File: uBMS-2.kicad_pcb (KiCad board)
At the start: 4 copper layers, 60 x 90 mm, 0 parts

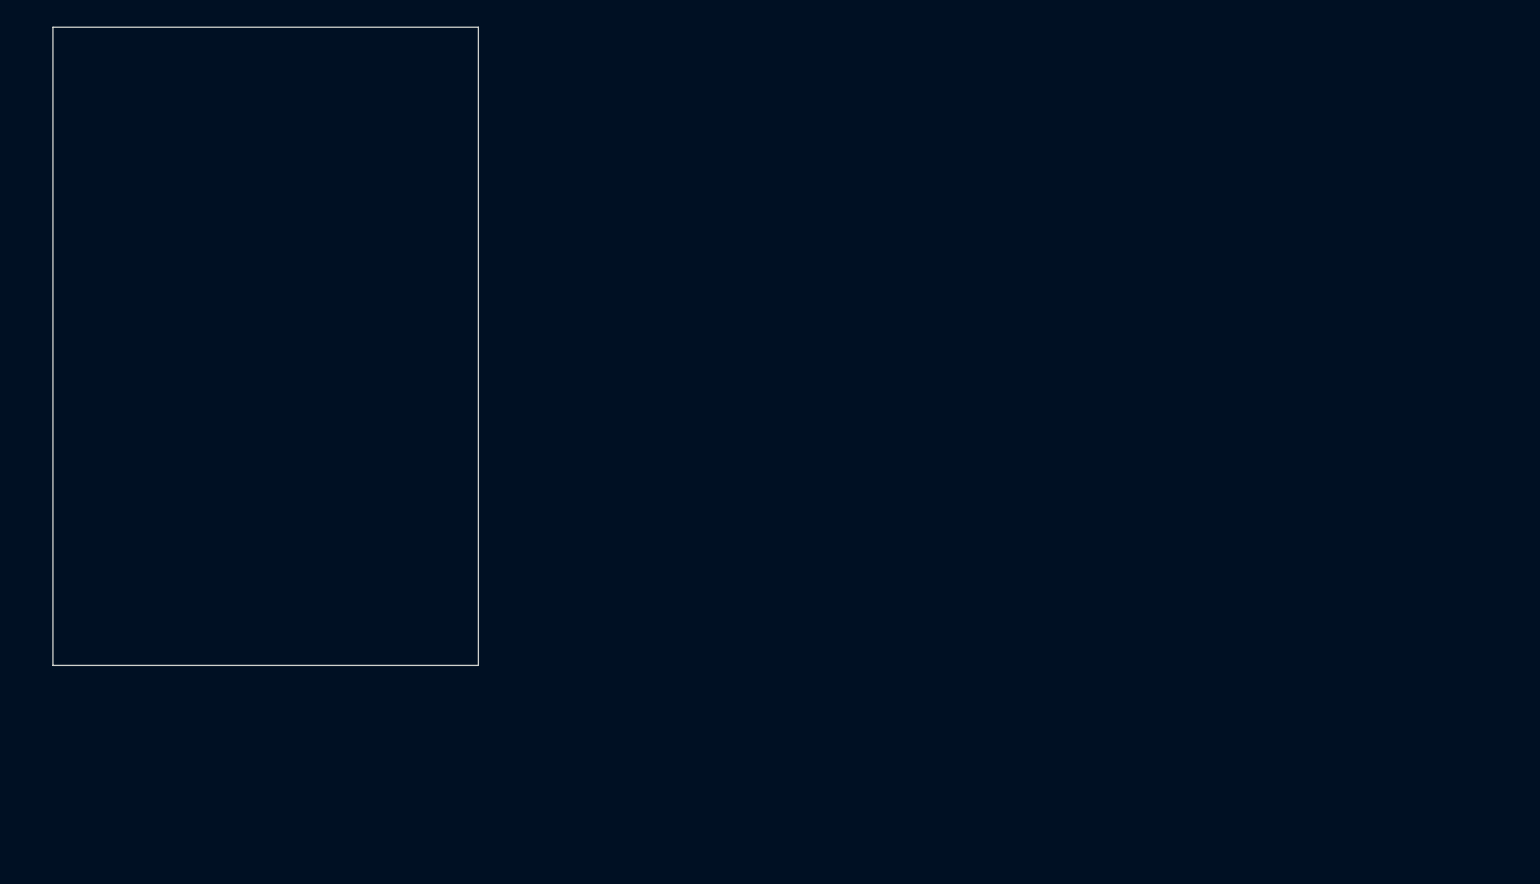
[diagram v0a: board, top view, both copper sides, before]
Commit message: Using Molex Milli Grid Connector for 14 pin
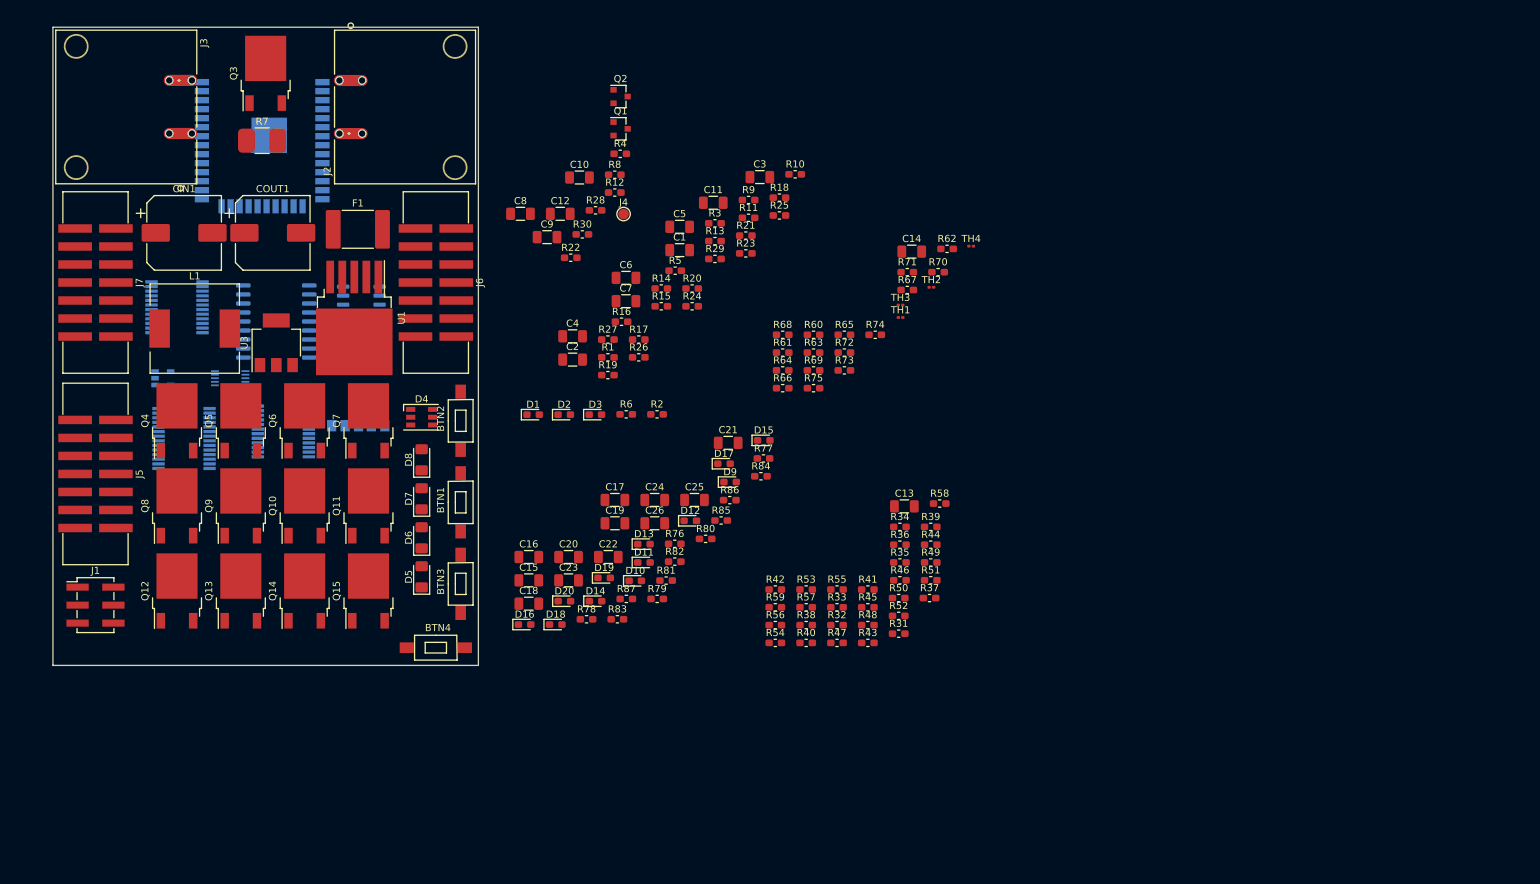
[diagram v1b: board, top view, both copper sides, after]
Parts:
- added BTN1: Reset, Button_Switch_SMD:PTS636_SM43_SMTR_LFS_6mm_3,5mm, F.Cu at (77.5, 87.0)
- added BTN2: Program, Button_Switch_SMD:PTS636_SM43_SMTR_LFS_6mm_3,5mm, F.Cu at (77.5, 75.5)
- added BTN3: Input_1, Button_Switch_SMD:PTS636_SM43_SMTR_LFS_6mm_3,5mm, F.Cu at (77.5, 98.5)
- added BTN4: Input_2, Button_Switch_SMD:PTS636_SM43_SMTR_LFS_6mm_3,5mm, F.Cu at (74.0, 107.5)
- added C1: 0.1uF, Capacitor_SMD:C_1206_3216Metric, F.Cu at (108.4, 51.4)
- added C10: 0.1uF, Capacitor_SMD:C_1206_3216Metric, F.Cu at (94.3, 41.2)
- added C11: 0.1uF, Capacitor_SMD:C_1206_3216Metric, F.Cu at (113.1, 44.8)
- added C12: 0.1uF, Capacitor_SMD:C_1206_3216Metric, F.Cu at (91.5, 46.3)
- added C13: 0.1uF, Capacitor_SMD:C_1206_3216Metric, F.Cu at (140.1, 87.6)
- added C14: 0.1uF, Capacitor_SMD:C_1206_3216Metric, F.Cu at (141.1, 51.6)
- added C15: 10nF, Capacitor_SMD:C_1206_3216Metric, F.Cu at (87.1, 98.0)
- added C16: 10nF, Capacitor_SMD:C_1206_3216Metric, F.Cu at (87.1, 94.7)
- added C17: 10nF, Capacitor_SMD:C_1206_3216Metric, F.Cu at (99.3, 86.7)
- added C18: 10nF, Capacitor_SMD:C_1206_3216Metric, F.Cu at (87.1, 101.3)
- added C19: 10nF, Capacitor_SMD:C_1206_3216Metric, F.Cu at (99.3, 90.0)
- added C2: 10uF, Capacitor_SMD:C_1206_3216Metric, F.Cu at (93.3, 66.9)
- added C20: 10nF, Capacitor_SMD:C_1206_3216Metric, F.Cu at (92.7, 94.7)
- added C21: 10nF, Capacitor_SMD:C_1206_3216Metric, F.Cu at (115.2, 78.6)
- added C22: 10nF, Capacitor_SMD:C_1206_3216Metric, F.Cu at (98.3, 94.7)
- added C23: 10nF, Capacitor_SMD:C_1206_3216Metric, F.Cu at (92.7, 98.0)
- added C24: 10nF, Capacitor_SMD:C_1206_3216Metric, F.Cu at (104.9, 86.7)
- added C25: 10nF, Capacitor_SMD:C_1206_3216Metric, F.Cu at (110.5, 86.7)
- added C26: 10nF, Capacitor_SMD:C_1206_3216Metric, F.Cu at (104.9, 90.0)
- added C3: 0.1uF, Capacitor_SMD:C_1206_3216Metric, F.Cu at (119.7, 41.1)
- added C4: 0.1uF, Capacitor_SMD:C_1206_3216Metric, F.Cu at (93.3, 63.6)
- added C5: 2.2uF, Capacitor_SMD:C_1206_3216Metric, F.Cu at (108.4, 48.1)
- added C6: 1uF, Capacitor_SMD:C_1206_3216Metric, F.Cu at (100.8, 55.3)
- added C7: 1uF, Capacitor_SMD:C_1206_3216Metric, F.Cu at (100.8, 58.6)
- added C8: 0.1uF, Capacitor_SMD:C_1206_3216Metric, F.Cu at (85.9, 46.3)
- added C9: 0.1uF, Capacitor_SMD:C_1206_3216Metric, F.Cu at (89.7, 49.6)
- added CIN1: 100uF 60V, Capacitor_SMD:CP_Elec_10x10, F.Cu at (38.5, 49.0)
- added COUT1: 1000uF, Capacitor_SMD:CP_Elec_10x10, F.Cu at (51.0, 49.0)
- added D1: D, Diode_SMD:D_0603_1608Metric_Pad1.05x0.95mm_HandSolder, F.Cu at (87.7, 74.6)
- added D10: D, Diode_SMD:D_0603_1608Metric_Pad1.05x0.95mm_HandSolder, F.Cu at (102.1, 98.1)
- added D11: D, Diode_SMD:D_0603_1608Metric_Pad1.05x0.95mm_HandSolder, F.Cu at (103.4, 95.5)
- added D12: D, Diode_SMD:D_0603_1608Metric_Pad1.05x0.95mm_HandSolder, F.Cu at (109.9, 89.6)
- added D13: D, Diode_SMD:D_0603_1608Metric_Pad1.05x0.95mm_HandSolder, F.Cu at (103.4, 92.9)
- added D14: D, Diode_SMD:D_0603_1608Metric_Pad1.05x0.95mm_HandSolder, F.Cu at (96.5, 100.9)
- added D15: D, Diode_SMD:D_0603_1608Metric_Pad1.05x0.95mm_HandSolder, F.Cu at (120.3, 78.3)
- added D16: D, Diode_SMD:D_0603_1608Metric_Pad1.05x0.95mm_HandSolder, F.Cu at (86.5, 104.2)
- added D17: D, Diode_SMD:D_0603_1608Metric_Pad1.05x0.95mm_HandSolder, F.Cu at (114.6, 81.6)
- added D18: D, Diode_SMD:D_0603_1608Metric_Pad1.05x0.95mm_HandSolder, F.Cu at (90.9, 104.2)
- added D19: D, Diode_SMD:D_0603_1608Metric_Pad1.05x0.95mm_HandSolder, F.Cu at (97.7, 97.7)
- added D2: D, Diode_SMD:D_0603_1608Metric_Pad1.05x0.95mm_HandSolder, F.Cu at (92.1, 74.6)
- added D20: D, Diode_SMD:D_0603_1608Metric_Pad1.05x0.95mm_HandSolder, F.Cu at (92.1, 100.9)
- added D3: D, Diode_SMD:D_0603_1608Metric_Pad1.05x0.95mm_HandSolder, F.Cu at (96.5, 74.6)
- added D4: CLX6F-FKC, LED_SMD:LED_RGB_PLCC-6, F.Cu at (72.0, 75.0)
- added D5: LED, LED_SMD:LED_1206_3216Metric_Pad1.42x1.75mm_HandSolder, F.Cu at (72.0, 97.5)
- added D6: LED, LED_SMD:LED_1206_3216Metric_Pad1.42x1.75mm_HandSolder, F.Cu at (72.0, 92.0)
- added D7: LED, LED_SMD:LED_1206_3216Metric_Pad1.42x1.75mm_HandSolder, F.Cu at (72.0, 86.5)
- added D8: LED, LED_SMD:LED_1206_3216Metric_Pad1.42x1.75mm_HandSolder, F.Cu at (72.0, 81.0)
- added D9: D, Diode_SMD:D_0603_1608Metric_Pad1.05x0.95mm_HandSolder, F.Cu at (115.5, 84.1)
- added F1: 1A PTC, Fuse:Fuse_2920_7451Metric_Pad2.10x5.45mm_HandSolder, F.Cu at (63.0, 48.5)
- added J1: Conn_02x03_Counter_Clockwise, Connector_PinHeader_2.54mm:PinHeader_2x03_P2.54mm_Vertical_SMD, F.Cu at (26.0, 101.5)
- added J2: Conn_01x02, uBMS-2:1720430202, F.Cu at (62.0, 35.0)
- added J3: Conn_01x02, uBMS-2:1720430202, F.Cu at (38.0, 27.5)
- added J4: Conn_01x01, TestPoint:TestPoint_Pad_D1.5mm, F.Cu at (100.5, 46.3)
- added J5: Conn_02x07_Counter_Clockwise, uBMS-2:CNC-Tech_3020-14-0300-00, F.Cu at (26.0, 83.0)
- added J6: Conn_02x07_Counter_Clockwise, uBMS-2:CNC-Tech_3020-14-0300-00, F.Cu at (74.0, 56.0)
- added J7: Conn_02x07_Counter_Clockwise, uBMS-2:CNC-Tech_3020-14-0300-00, F.Cu at (26.0, 56.0)
- added L1: 100uH, Inductor_SMD:L_12x12mm_H8mm, F.Cu at (40.0, 62.5)
- added Q1: 2N7002, Package_TO_SOT_SMD:SOT-23, F.Cu at (100.1, 34.3)
- added Q10: FQD5N20L, Package_TO_SOT_SMD:TO-252-2, F.Cu at (55.5, 87.5)
- added Q11: FQD5N20L, Package_TO_SOT_SMD:TO-252-2, F.Cu at (64.5, 87.5)
- added Q12: FQD5N20L, Package_TO_SOT_SMD:TO-252-2, F.Cu at (37.5, 99.5)
- added Q13: FQD5N20L, Package_TO_SOT_SMD:TO-252-2, F.Cu at (46.5, 99.5)
- added Q14: FQD5N20L, Package_TO_SOT_SMD:TO-252-2, F.Cu at (55.5, 99.5)
- added Q15: FQD5N20L, Package_TO_SOT_SMD:TO-252-2, F.Cu at (64.5, 99.5)
- added Q2: 2N7002, Package_TO_SOT_SMD:SOT-23, F.Cu at (100.1, 29.8)
- added Q3: NTD5865NL, Package_TO_SOT_SMD:TO-252-2, F.Cu at (50.0, 26.5)
- added Q4: FQD5N20L, Package_TO_SOT_SMD:TO-252-2, F.Cu at (37.5, 75.5)
- added Q5: FQD5N20L, Package_TO_SOT_SMD:TO-252-2, F.Cu at (46.5, 75.5)
- added Q6: FQD5N20L, Package_TO_SOT_SMD:TO-252-2, F.Cu at (55.5, 75.5)
- added Q7: FQD5N20L, Package_TO_SOT_SMD:TO-252-2, F.Cu at (64.5, 75.5)
- added Q8: FQD5N20L, Package_TO_SOT_SMD:TO-252-2, F.Cu at (37.5, 87.5)
- added Q9: FQD5N20L, Package_TO_SOT_SMD:TO-252-2, F.Cu at (46.5, 87.5)
- added R1: 2.2k, Resistor_SMD:R_0603_1608Metric_Pad1.05x0.95mm_HandSolder, F.Cu at (98.3, 66.6)
- added R10: 330R, Resistor_SMD:R_0603_1608Metric_Pad1.05x0.95mm_HandSolder, F.Cu at (124.7, 40.7)
- added R11: 270R, Resistor_SMD:R_0603_1608Metric_Pad1.05x0.95mm_HandSolder, F.Cu at (118.1, 46.9)
- added R12: 270R, Resistor_SMD:R_0603_1608Metric_Pad1.05x0.95mm_HandSolder, F.Cu at (99.2, 43.3)
- added R13: 270R, Resistor_SMD:R_0603_1608Metric_Pad1.05x0.95mm_HandSolder, F.Cu at (113.4, 50.2)
- added R14: 270R, Resistor_SMD:R_0603_1608Metric_Pad1.05x0.95mm_HandSolder, F.Cu at (105.8, 56.8)
- added R15: 270R, Resistor_SMD:R_0603_1608Metric_Pad1.05x0.95mm_HandSolder, F.Cu at (105.8, 59.4)
- added R16: 270R, Resistor_SMD:R_0603_1608Metric_Pad1.05x0.95mm_HandSolder, F.Cu at (100.2, 61.5)
- added R17: 270R, Resistor_SMD:R_0603_1608Metric_Pad1.05x0.95mm_HandSolder, F.Cu at (102.6, 64.0)
- added R18: 270R, Resistor_SMD:R_0603_1608Metric_Pad1.05x0.95mm_HandSolder, F.Cu at (122.5, 44.0)
- added R19: 4.7k, Resistor_SMD:R_0603_1608Metric_Pad1.05x0.95mm_HandSolder, F.Cu at (98.3, 69.1)
- added R2: 2.2k, Resistor_SMD:R_0603_1608Metric_Pad1.05x0.95mm_HandSolder, F.Cu at (105.2, 74.6)
- added R20: 4.7k, Resistor_SMD:R_0603_1608Metric_Pad1.05x0.95mm_HandSolder, F.Cu at (110.1, 56.8)
- added R21: 4.7k, Resistor_SMD:R_0603_1608Metric_Pad1.05x0.95mm_HandSolder, F.Cu at (117.7, 49.4)
- added R22: 270R, Resistor_SMD:R_0603_1608Metric_Pad1.05x0.95mm_HandSolder, F.Cu at (93.0, 52.5)
- added R23: 270R, Resistor_SMD:R_0603_1608Metric_Pad1.05x0.95mm_HandSolder, F.Cu at (117.7, 51.9)
- added R24: 270R, Resistor_SMD:R_0603_1608Metric_Pad1.05x0.95mm_HandSolder, F.Cu at (110.1, 59.4)
- added R25: 270R, Resistor_SMD:R_0603_1608Metric_Pad1.05x0.95mm_HandSolder, F.Cu at (122.5, 46.5)
- added R26: 270R, Resistor_SMD:R_0603_1608Metric_Pad1.05x0.95mm_HandSolder, F.Cu at (102.6, 66.6)
- added R27: 270R, Resistor_SMD:R_0603_1608Metric_Pad1.05x0.95mm_HandSolder, F.Cu at (98.3, 64.0)
- added R28: 270R, Resistor_SMD:R_0603_1608Metric_Pad1.05x0.95mm_HandSolder, F.Cu at (96.5, 45.8)
- added R29: 4.7k, Resistor_SMD:R_0603_1608Metric_Pad1.05x0.95mm_HandSolder, F.Cu at (113.4, 52.7)
- added R3: 10k, Resistor_SMD:R_0603_1608Metric_Pad1.05x0.95mm_HandSolder, F.Cu at (113.4, 47.7)
- added R30: 4.7k, Resistor_SMD:R_0603_1608Metric_Pad1.05x0.95mm_HandSolder, F.Cu at (94.7, 49.2)
- added R31: 360k, Resistor_SMD:R_0603_1608Metric_Pad1.05x0.95mm_HandSolder, F.Cu at (139.3, 105.5)
- added R32: 200k, Resistor_SMD:R_0603_1608Metric_Pad1.05x0.95mm_HandSolder, F.Cu at (130.6, 104.3)
- added R33: 330k, Resistor_SMD:R_0603_1608Metric_Pad1.05x0.95mm_HandSolder, F.Cu at (130.6, 101.8)
- added R34: 500k, Resistor_SMD:R_0603_1608Metric_Pad1.05x0.95mm_HandSolder, F.Cu at (139.4, 90.5)
- added R35: 500k, Resistor_SMD:R_0603_1608Metric_Pad1.05x0.95mm_HandSolder, F.Cu at (139.4, 95.5)
- added R36: 560k, Resistor_SMD:R_0603_1608Metric_Pad1.05x0.95mm_HandSolder, F.Cu at (139.4, 93.0)
- added R37: 360k, Resistor_SMD:R_0603_1608Metric_Pad1.05x0.95mm_HandSolder, F.Cu at (143.6, 100.5)
- added R38: 100k, Resistor_SMD:R_0603_1608Metric_Pad1.05x0.95mm_HandSolder, F.Cu at (126.2, 104.3)
- added R39: 100k, Resistor_SMD:R_0603_1608Metric_Pad1.05x0.95mm_HandSolder, F.Cu at (143.8, 90.5)
- added R4: 10k, Resistor_SMD:R_0603_1608Metric_Pad1.05x0.95mm_HandSolder, F.Cu at (100.0, 37.9)
- added R40: 100k, Resistor_SMD:R_0603_1608Metric_Pad1.05x0.95mm_HandSolder, F.Cu at (126.2, 106.8)
- added R41: 100k, Resistor_SMD:R_0603_1608Metric_Pad1.05x0.95mm_HandSolder, F.Cu at (134.9, 99.3)
- added R42: 47k, Resistor_SMD:R_0603_1608Metric_Pad1.05x0.95mm_HandSolder, F.Cu at (121.9, 99.3)
- added R43: 25k, Resistor_SMD:R_0603_1608Metric_Pad1.05x0.95mm_HandSolder, F.Cu at (134.9, 106.8)
- added R44: 47k, Resistor_SMD:R_0603_1608Metric_Pad1.05x0.95mm_HandSolder, F.Cu at (143.8, 93.0)
- added R45: 560k, Resistor_SMD:R_0603_1608Metric_Pad1.05x0.95mm_HandSolder, F.Cu at (134.9, 101.8)
- added R46: 500k, Resistor_SMD:R_0603_1608Metric_Pad1.05x0.95mm_HandSolder, F.Cu at (139.4, 98.0)
- added R47: 560k, Resistor_SMD:R_0603_1608Metric_Pad1.05x0.95mm_HandSolder, F.Cu at (130.6, 106.8)
- added R48: 330k, Resistor_SMD:R_0603_1608Metric_Pad1.05x0.95mm_HandSolder, F.Cu at (134.9, 104.3)
- added R49: 500k, Resistor_SMD:R_0603_1608Metric_Pad1.05x0.95mm_HandSolder, F.Cu at (143.8, 95.5)
- added R5: 2.2k, Resistor_SMD:R_0603_1608Metric_Pad1.05x0.95mm_HandSolder, F.Cu at (107.8, 54.3)
- added R50: 147k, Resistor_SMD:R_0603_1608Metric_Pad1.05x0.95mm_HandSolder, F.Cu at (139.3, 100.5)
- added R51: 39.2k, Resistor_SMD:R_0603_1608Metric_Pad1.05x0.95mm_HandSolder, F.Cu at (143.8, 98.0)
- added R52: 30k, Resistor_SMD:R_0603_1608Metric_Pad1.05x0.95mm_HandSolder, F.Cu at (139.3, 103.0)
- added R53: 30k, Resistor_SMD:R_0603_1608Metric_Pad1.05x0.95mm_HandSolder, F.Cu at (126.2, 99.3)
- added R54: 30k, Resistor_SMD:R_0603_1608Metric_Pad1.05x0.95mm_HandSolder, F.Cu at (121.9, 106.8)
- added R55: 39.2k, Resistor_SMD:R_0603_1608Metric_Pad1.05x0.95mm_HandSolder, F.Cu at (130.6, 99.3)
- added R56: 33.2k, Resistor_SMD:R_0603_1608Metric_Pad1.05x0.95mm_HandSolder, F.Cu at (121.9, 104.3)
- added R57: 33.2k, Resistor_SMD:R_0603_1608Metric_Pad1.05x0.95mm_HandSolder, F.Cu at (126.2, 101.8)
- added R58: 16.2k, Resistor_SMD:R_0603_1608Metric_Pad1.05x0.95mm_HandSolder, F.Cu at (145.1, 87.2)
- added R59: 47.5k, Resistor_SMD:R_0603_1608Metric_Pad1.05x0.95mm_HandSolder, F.Cu at (121.9, 101.8)
- added R6: 2.2k, Resistor_SMD:R_0603_1608Metric_Pad1.05x0.95mm_HandSolder, F.Cu at (100.8, 74.6)
- added R60: 22k, Resistor_SMD:R_0603_1608Metric_Pad1.05x0.95mm_HandSolder, F.Cu at (127.3, 63.4)
- added R61: 22k, Resistor_SMD:R_0603_1608Metric_Pad1.05x0.95mm_HandSolder, F.Cu at (122.9, 65.9)
- added R62: 22k, Resistor_SMD:R_0603_1608Metric_Pad1.05x0.95mm_HandSolder, F.Cu at (146.1, 51.3)
- added R63: 22k, Resistor_SMD:R_0603_1608Metric_Pad1.05x0.95mm_HandSolder, F.Cu at (127.3, 65.9)
- added R64: 22k, Resistor_SMD:R_0603_1608Metric_Pad1.05x0.95mm_HandSolder, F.Cu at (122.9, 68.4)
- added R65: 22k, Resistor_SMD:R_0603_1608Metric_Pad1.05x0.95mm_HandSolder, F.Cu at (131.6, 63.4)
- added R66: 22k, Resistor_SMD:R_0603_1608Metric_Pad1.05x0.95mm_HandSolder, F.Cu at (122.9, 70.9)
- added R67: 22k, Resistor_SMD:R_0603_1608Metric_Pad1.05x0.95mm_HandSolder, F.Cu at (140.5, 57.1)
- added R68: 22k, Resistor_SMD:R_0603_1608Metric_Pad1.05x0.95mm_HandSolder, F.Cu at (122.9, 63.4)
- added R69: 22k, Resistor_SMD:R_0603_1608Metric_Pad1.05x0.95mm_HandSolder, F.Cu at (127.3, 68.4)
- added R7: 1m Ohm, Resistor_SMD:R_2512_CSNL2512, F.Cu at (49.5, 36.0)
- added R70: 22k, Resistor_SMD:R_0603_1608Metric_Pad1.05x0.95mm_HandSolder, F.Cu at (144.8, 54.5)
- added R71: 22k, Resistor_SMD:R_0603_1608Metric_Pad1.05x0.95mm_HandSolder, F.Cu at (140.5, 54.5)
- added R72: 4.7k, Resistor_SMD:R_0603_1608Metric_Pad1.05x0.95mm_HandSolder, F.Cu at (131.6, 65.9)
- added R73: 4.7k, Resistor_SMD:R_0603_1608Metric_Pad1.05x0.95mm_HandSolder, F.Cu at (131.6, 68.4)
- added R74: 4.7k, Resistor_SMD:R_0603_1608Metric_Pad1.05x0.95mm_HandSolder, F.Cu at (136.0, 63.4)
- added R75: 4.7k, Resistor_SMD:R_0603_1608Metric_Pad1.05x0.95mm_HandSolder, F.Cu at (127.3, 70.9)
- added R76: 100k, Resistor_SMD:R_0603_1608Metric_Pad1.05x0.95mm_HandSolder, F.Cu at (107.7, 92.9)
- added R77: 100k, Resistor_SMD:R_0603_1608Metric_Pad1.05x0.95mm_HandSolder, F.Cu at (120.2, 80.8)
- added R78: 100k, Resistor_SMD:R_0603_1608Metric_Pad1.05x0.95mm_HandSolder, F.Cu at (95.3, 103.5)
- added R79: 100k, Resistor_SMD:R_0603_1608Metric_Pad1.05x0.95mm_HandSolder, F.Cu at (105.2, 100.6)
- added R8: 470R, Resistor_SMD:R_0603_1608Metric_Pad1.05x0.95mm_HandSolder, F.Cu at (99.2, 40.8)
- added R80: 100k, Resistor_SMD:R_0603_1608Metric_Pad1.05x0.95mm_HandSolder, F.Cu at (112.0, 92.2)
- added R81: 100k, Resistor_SMD:R_0603_1608Metric_Pad1.05x0.95mm_HandSolder, F.Cu at (106.5, 98.0)
- added R82: 100k, Resistor_SMD:R_0603_1608Metric_Pad1.05x0.95mm_HandSolder, F.Cu at (107.7, 95.4)
- added R83: 100k, Resistor_SMD:R_0603_1608Metric_Pad1.05x0.95mm_HandSolder, F.Cu at (99.6, 103.5)
- added R84: 100k, Resistor_SMD:R_0603_1608Metric_Pad1.05x0.95mm_HandSolder, F.Cu at (119.8, 83.3)
- added R85: 100k, Resistor_SMD:R_0603_1608Metric_Pad1.05x0.95mm_HandSolder, F.Cu at (114.2, 89.6)
- added R86: 100k, Resistor_SMD:R_0603_1608Metric_Pad1.05x0.95mm_HandSolder, F.Cu at (115.5, 86.7)
- added R87: 100k, Resistor_SMD:R_0603_1608Metric_Pad1.05x0.95mm_HandSolder, F.Cu at (100.9, 100.6)
- added R9: 4.7k, Resistor_SMD:R_0603_1608Metric_Pad1.05x0.95mm_HandSolder, F.Cu at (118.1, 44.4)
- added TH1: 10k, Resistor_SMD:R_0201_0603Metric, F.Cu at (139.5, 60.9)
- added TH2: 10k, Resistor_SMD:R_0201_0603Metric, F.Cu at (143.9, 56.7)
- added TH3: 10k, Resistor_SMD:R_0201_0603Metric, F.Cu at (139.5, 59.2)
- added TH4: 10k, Resistor_SMD:R_0201_0603Metric, F.Cu at (149.5, 50.9)
- added U1: LM2576HVS-5, Package_TO_SOT_SMD:TO-263-5_TabPin3, F.Cu at (62.5, 61.0)
- added U10: CD74HC4067SM, Package_SO:SSOP-24_5.3x8.2mm_P0.65mm, B.Cu at (37.5, 59.5)
- added U11: CD74HC4067SM, Package_SO:SSOP-24_5.3x8.2mm_P0.65mm, B.Cu at (52.5, 77.0)
- added U2: ADS1115IDGS, Package_SO:TSSOP-10_3x3mm_P0.5mm, B.Cu at (45.0, 69.5)
- added U3: TLV1117-33, Package_TO_SOT_SMD:SOT-223-3_TabPin2, F.Cu at (51.5, 64.5)
- added U4: TL431DBV, Package_TO_SOT_SMD:SOT-23-5, B.Cu at (35.5, 69.5)
- added U5: ESP32-WROOM-32, RF_Module:ESP32-WROOM-32, B.Cu at (49.5, 36.0)
- added U6: TSC2012IDT, Package_SO:SO-8_3.9x4.9mm_P1.27mm, B.Cu at (63.5, 58.5)
- added U7: MCP23017_SS, Package_SO:SSOP-28_5.3x10.2mm_P0.65mm, B.Cu at (38.5, 78.0)
- added U8: MCP23008-E_P, Package_SO:SOIC-18W_7.5x11.6mm_P1.27mm, B.Cu at (51.5, 61.5)
- added U9: VDMG10C0, Display_7Segment:VDMG10C0, B.Cu at (63.0, 69.5)

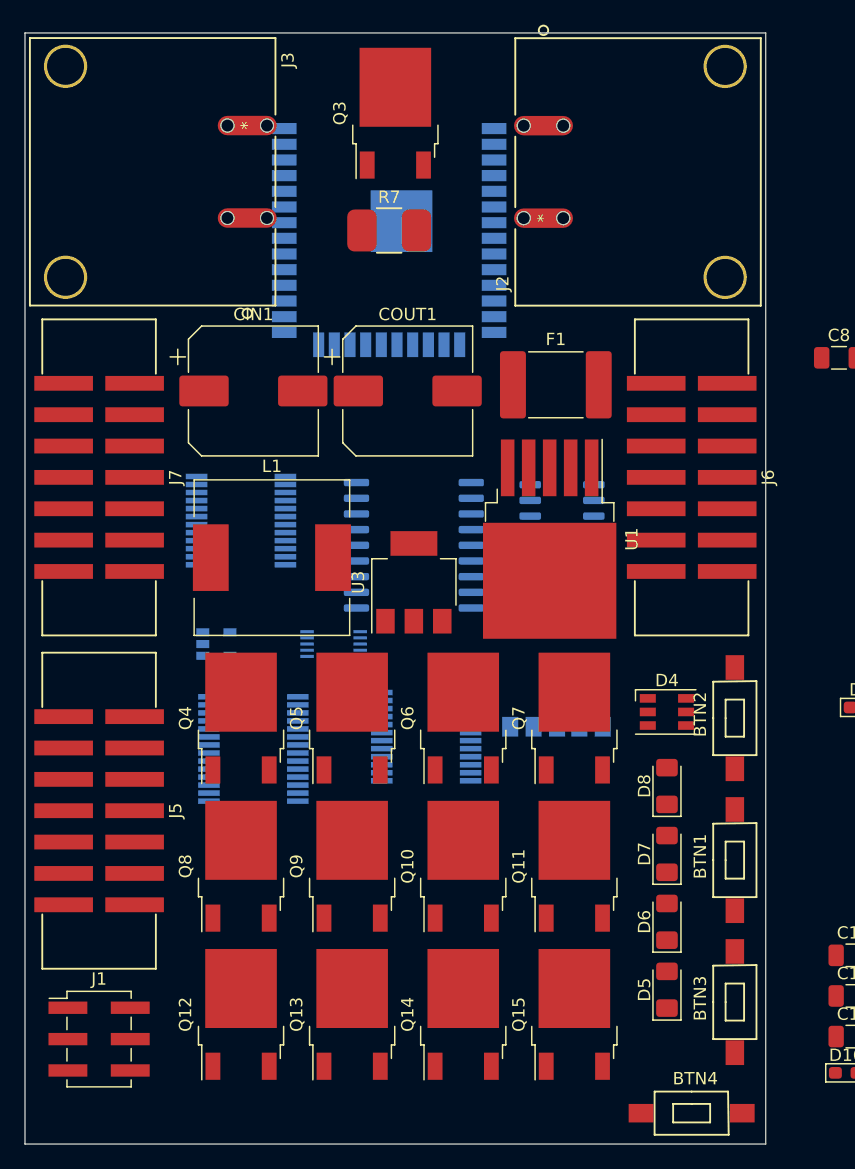
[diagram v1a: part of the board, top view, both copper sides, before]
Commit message: Fixed power connector footprint and 3d
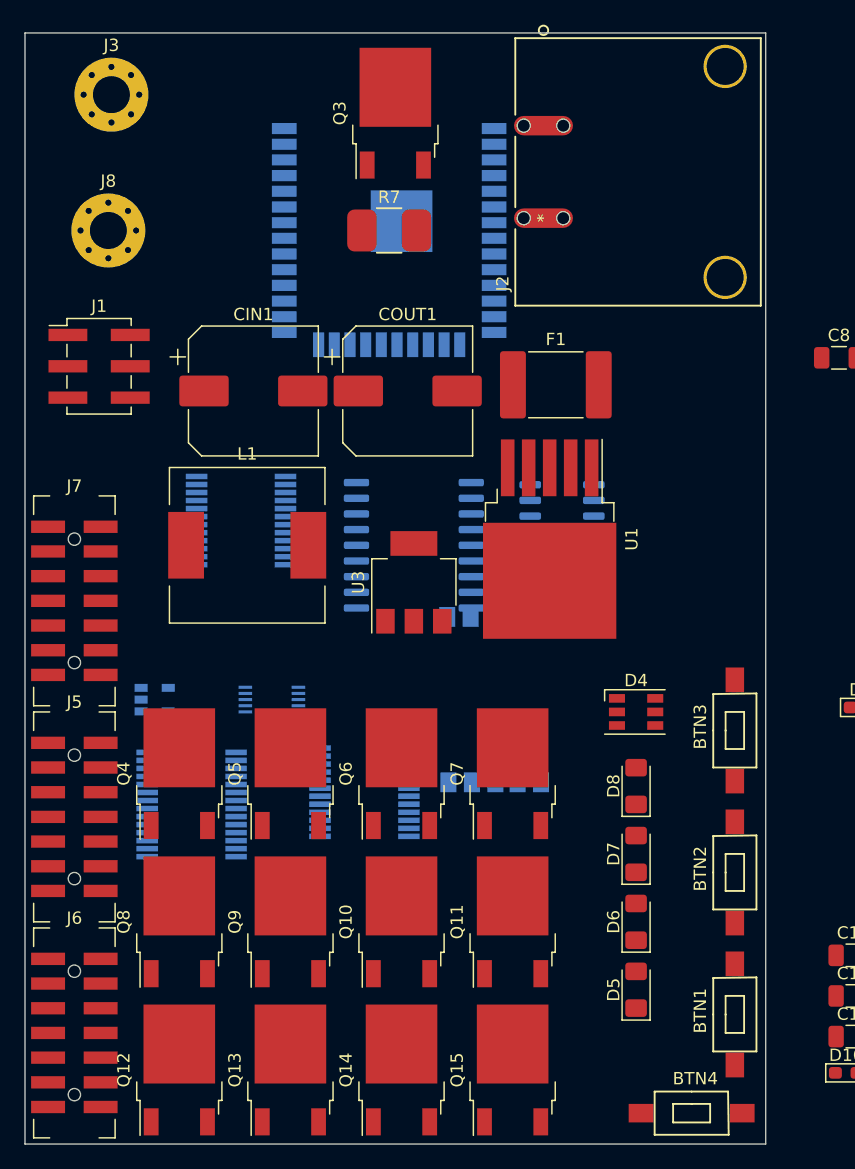
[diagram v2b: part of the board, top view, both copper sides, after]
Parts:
- added J8: Conn_01x01, MountingHole:MountingHole_3mm_Pad_Via, F.Cu at (26.8, 36.0)
- J3: value Conn_01x02 -> Conn_01x01; footprint uBMS-2:1720430202 -> MountingHole:MountingHole_3mm_Pad_Via
- J5, J6, J7: footprint uBMS-2:CNC-Tech_3020-14-0300-00 -> uBMS-2:Molex_Milli_Grid_0878325623
- moved J6 67.3 mm to (24.0, 101.0)
- moved J1 54.5 mm to (26.0, 47.0)
- moved BTN3 22.0 mm to (77.5, 76.5)
- moved BTN1 12.5 mm to (77.5, 99.5)
- moved BTN2 12.5 mm to (77.5, 88.0)
- moved J3 11.3 mm to (27.0, 25.0), turned to 0 degrees
- moved J7 10.2 mm to (24.0, 66.0)
- moved Q10 6.73 mm to (50.5, 92.0)
- moved Q11 6.73 mm to (59.5, 92.0)
- moved Q12 6.73 mm to (32.5, 104.0)
- moved Q13 6.73 mm to (41.5, 104.0)
- moved Q14 6.73 mm to (50.5, 104.0)
- moved Q15 6.73 mm to (59.5, 104.0)
- moved Q4 6.73 mm to (32.5, 80.0)
- moved Q5 6.73 mm to (41.5, 80.0)
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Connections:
- J3 pad 1: GND -> /Batt_Pos
